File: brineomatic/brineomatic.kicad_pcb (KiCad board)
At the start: 4 copper layers, 106 x 66.5 mm, 168 parts, among them J1 Conn_01x04_MountingPin, J10 5.08MM, J12 3.5MM, J14 3.5MM, J16 3.5MM, J19 USB_TYPE_C_16PIN, J20 Conn_01x04, J22 3.5mm, J24 3.5MM, J7 3.5MM, Q1 AO3400A, Q2 AO3400A, Q3 20N06, Q4 AO3400A, Q5 AO3400A, Q6 AO3400A, Q7 AO3400A, SW1 RESET, SW2 BOOT, U1 ADS1115IDGSR, U2 LM74700, U3 XL1509-5.0, U4 ESP32-S3-WROOM-1-N16R8, U5 USBLC6-2SC6, U6 SN74LV1T34DBV, U7 XC6210B332MR, U8 TMC2209-LA, U9 MAX3485

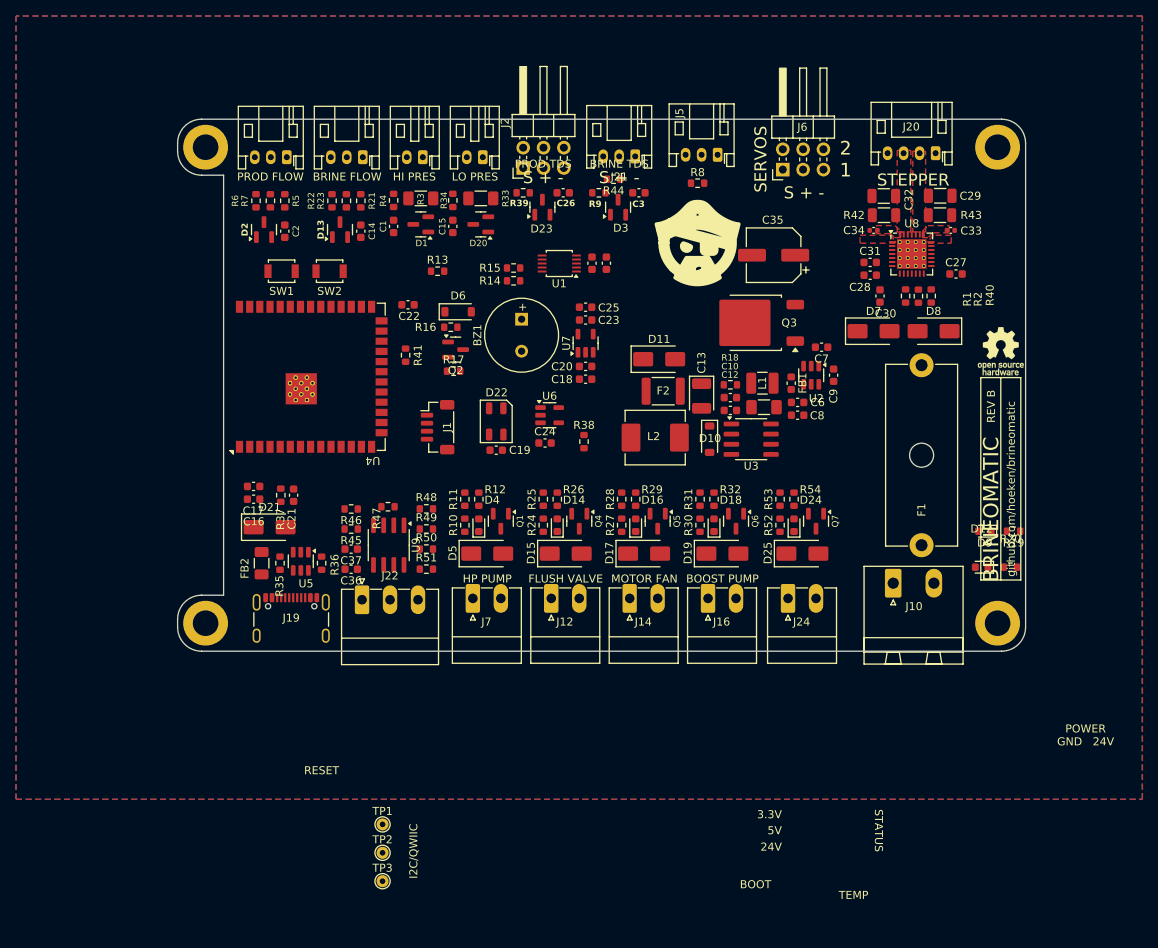
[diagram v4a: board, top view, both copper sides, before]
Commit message: all connectors are now flush withe 3mm outside edge of the case
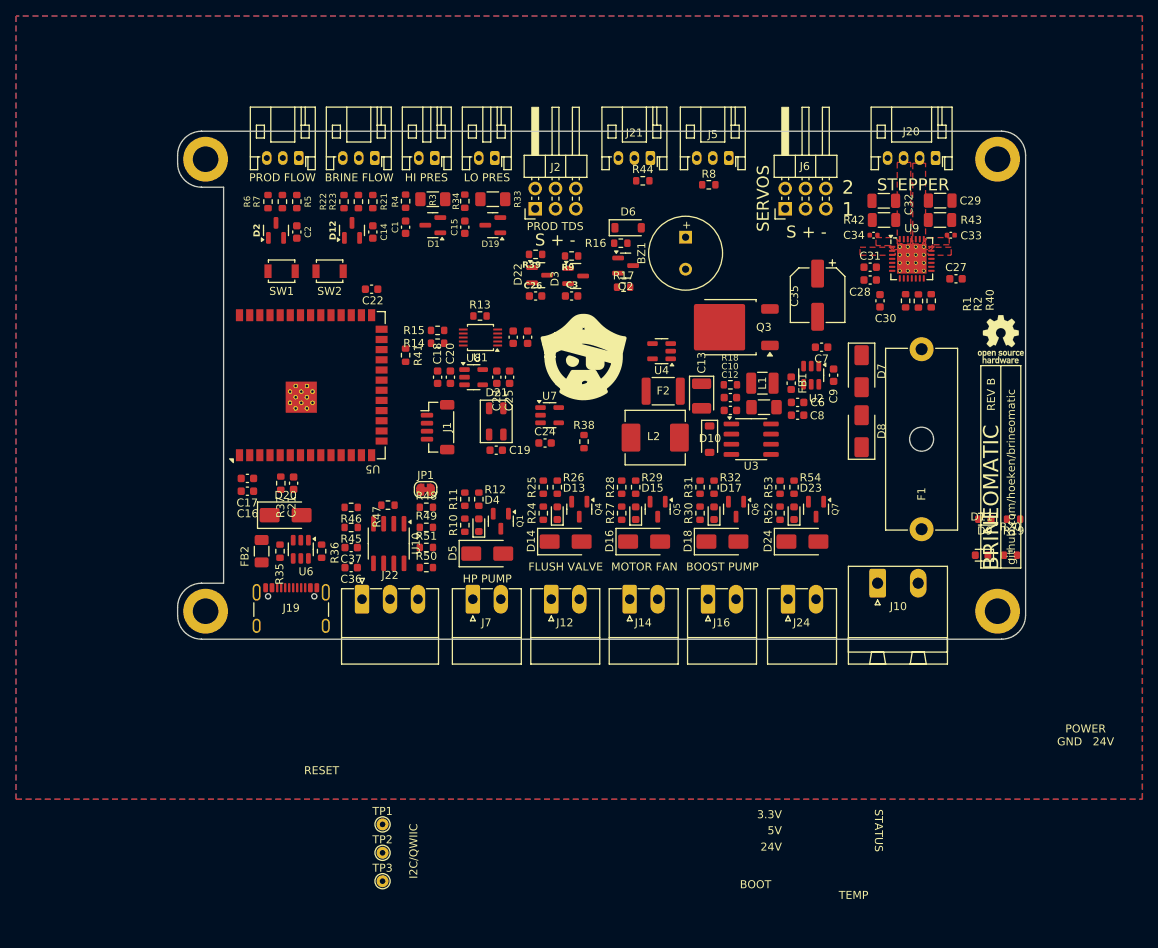
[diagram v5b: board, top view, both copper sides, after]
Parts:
- removed the D11 at (123.2, 57.5)
- added JP1: SolderJumper_2_Bridged, Jumper:SolderJumper-2_P1.3mm_Bridged_RoundedPad1.0x1.5mm, F.Cu at (94.0, 73.8)
- added U4: MAX40200AUK, Package_TO_SOT_SMD:SOT-23-5, F.Cu at (123.5, 56.5)
- moved D6 23.7 mm to (119.3, 41.1)
- moved Q2 23.7 mm to (119.0, 45.8)
- moved R16 23.7 mm to (118.4, 43.0)
- moved R17 23.7 mm to (118.8, 48.5)
- moved BZ1 22.9 mm to (126.5, 44.2)
- moved SYM2 20.2 mm to (113.8, 57.2)
- moved C18 18.5 mm to (95.5, 59.8), turned to -90 degrees
- moved C20 17.0 mm to (97.1, 59.8), turned to -90 degrees
- moved D8 15.4 mm to (148.5, 66.5), turned to 90 degrees
- moved C3 15.4 mm to (112.2, 49.6), turned to 180 degrees
- moved U8 14.6 mm to (100.0, 59.8), turned to 0 degrees
- moved C4 13.5 mm to (105.0, 54.8)
- moved C5 13.5 mm to (106.8, 54.8)
- moved U1 13.5 mm to (100.9, 54.8)
- moved C26 13.4 mm to (107.8, 49.6), turned to 180 degrees
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- renumbered D12 to D11, D13 to D12, D14 to D13, D15 to D14, D16 to D15, D17 to D16, D18 to D17, D19 to D18, D20 to D19, D21 to D20, D22 to D21, D23 to D22, D24 to D23, D25 to D24, R51 to R50, R50 to R51, U9 to U10, U4 to U5, U5 to U6, U6 to U7, U7 to U8, U8 to U9
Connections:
- C13 pad 1: 5V_TRUE -> 5V_HIGH_POWER
- F2 pad 1: 5V_TRUE -> 5V_HIGH_POWER
- J11 pad 1: 5V_TRUE -> +5V
- J2 pad 3: 5V_TRUE -> +5V
- J2 pad 4: 5V_TRUE -> +5V
- J4 pad 1: 5V_TRUE -> +5V
- J6 pad 3: 5V_TRUE -> 5V_HIGH_POWER
- J6 pad 4: 5V_TRUE -> 5V_HIGH_POWER
- R21 pad 2: 5V_TRUE -> +5V
- R5 pad 2: 5V_TRUE -> +5V
- R51 pad 2: Net-(J22-Pin_1) -> Net-(JP1-A)
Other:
- board size 106 x 66.5 mm -> 106 x 63.5 mm
- board text removed: "BRINE TDS"

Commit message: connector placement done
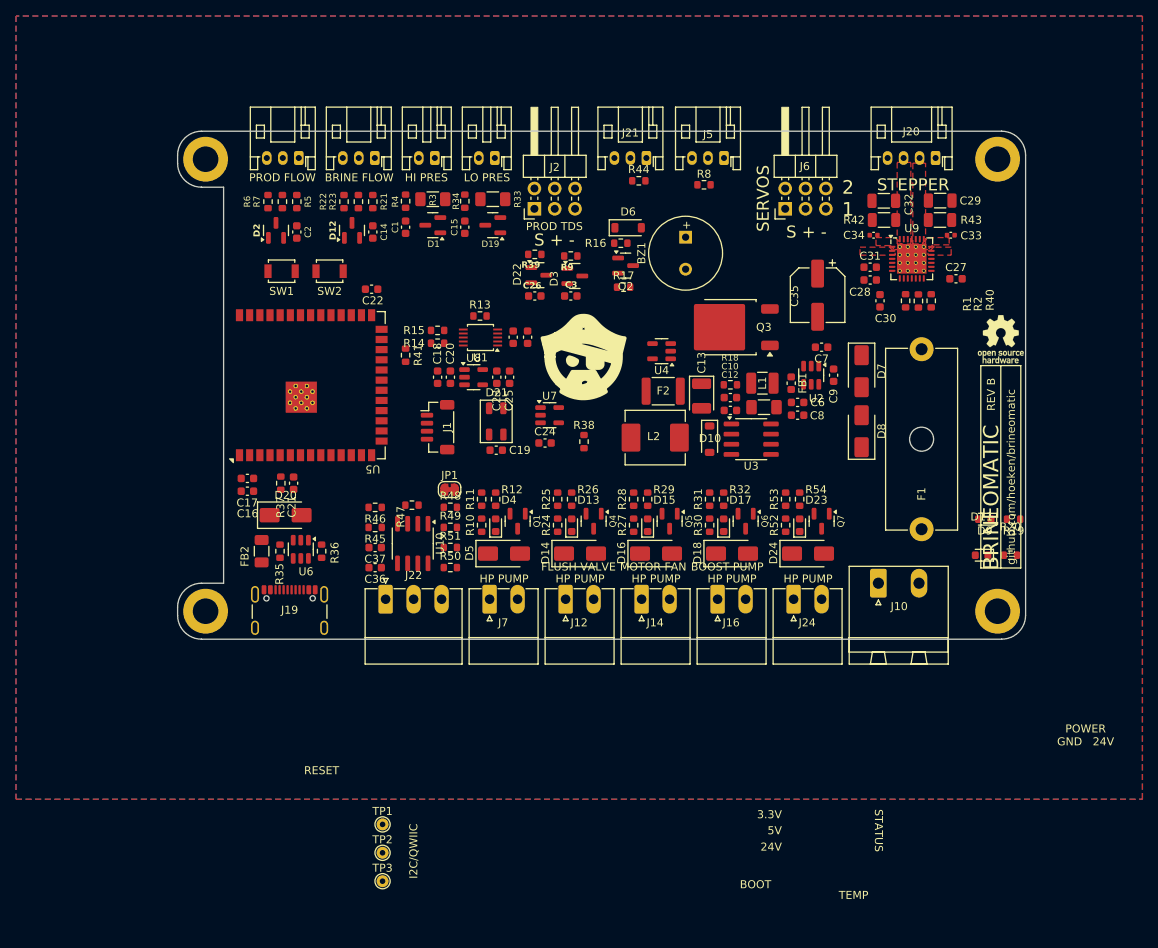
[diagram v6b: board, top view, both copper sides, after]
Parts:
- moved C36 3.00 mm to (87.7, 83.6)
- moved C37 3.00 mm to (87.7, 81.0)
- moved JP1 3.00 mm to (97.0, 73.8)
- moved R45 3.00 mm to (87.7, 78.5)
- moved R46 3.00 mm to (87.7, 76.0)
- moved R47 3.00 mm to (92.3, 75.7)
- moved R48 3.00 mm to (97.1, 76.0)
- moved R49 3.00 mm to (97.1, 78.5)
- moved R50 3.00 mm to (97.1, 83.5)
- moved R51 3.00 mm to (97.1, 81.0)
- moved U10 3.00 mm to (92.4, 80.5)
- moved J22 2.94 mm to (89.0, 87.5)
- moved D13 2.34 mm to (112.3, 78.2)
- moved D14 2.34 mm to (113.3, 81.8)
- moved Q4 2.34 mm to (115.0, 77.8)
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
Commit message: schematic tidy, usb c position verified, component placement work.
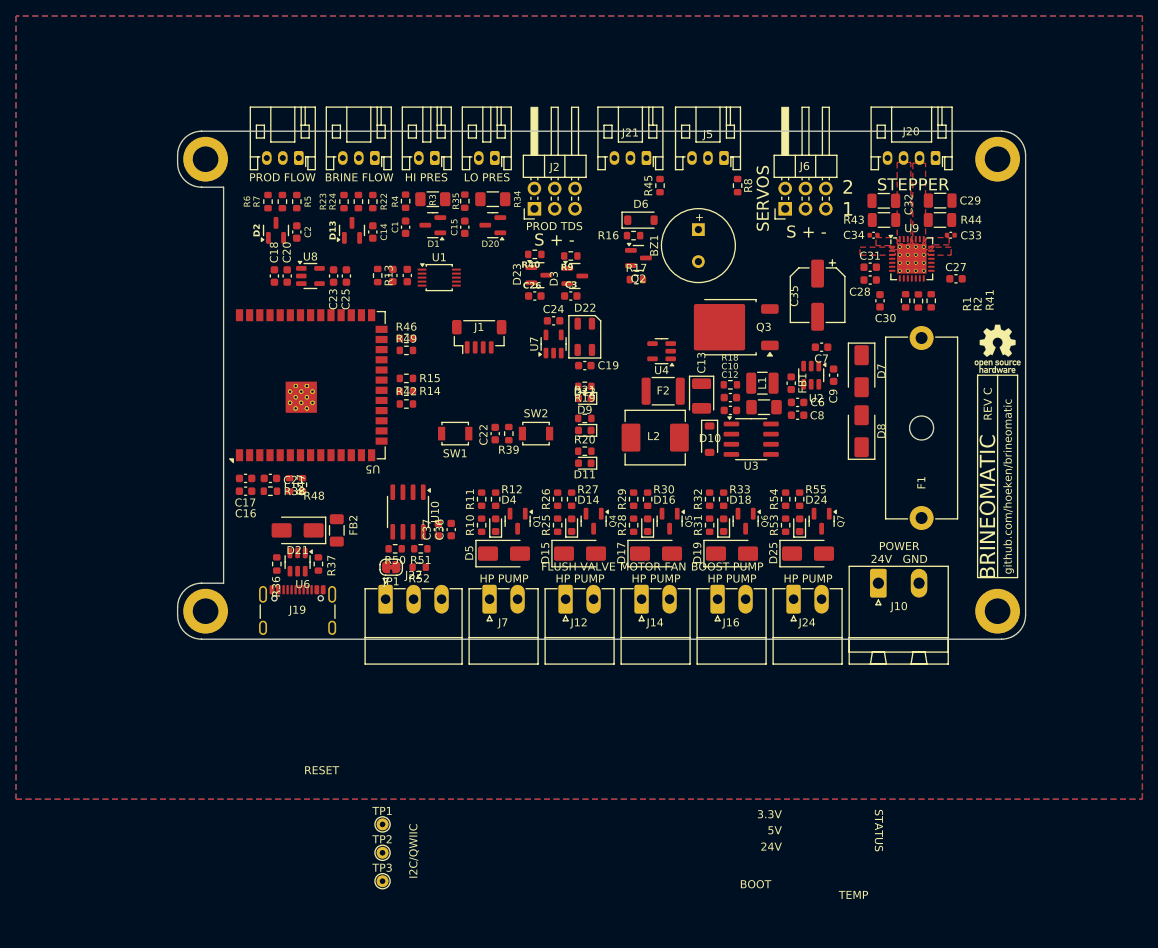
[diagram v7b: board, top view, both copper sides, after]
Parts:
- removed SYM2: Logo_Open_Hardware_Small, yarrboard:Logo Small
- added D11: GREEN, LED_SMD:LED_0603_1608Metric, F.Cu at (113.9, 70.5)
- added R20: 10k, Resistor_SMD:R_0603_1608Metric, F.Cu at (113.9, 69.0)
- R50: renamed from R49; value 10k -> 20k
- R51: renamed from R50; value 10k -> 20k
- moved R19 56.1 mm to (113.9, 60.9)
- moved R21 55.9 mm to (113.9, 64.9)
- moved D9 52.2 mm to (113.9, 62.4)
- moved D12 52.0 mm to (113.9, 66.4)
- moved SW2 32.8 mm to (107.8, 66.8), turned to 0 degrees
- moved SW1 29.7 mm to (97.7, 66.8)
- moved C18 24.0 mm to (75.1, 47.1)
- moved C23 24.0 mm to (82.5, 47.1)
- moved C25 24.0 mm to (84.1, 47.1)
- moved U8 24.0 mm to (79.6, 47.1)
- moved C20 24.0 mm to (76.7, 47.1)
- moved R46 24.0 mm to (91.6, 54.9), turned to 0 degrees
- moved C22 23.8 mm to (102.7, 66.8), turned to 90 degrees
- moved R49 20.4 mm to (91.6, 56.4)
- moved C5 18.5 mm to (89.9, 47.0), turned to -90 degrees
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- renumbered D11 to D12, D12 to D13, D13 to D14, D14 to D15, D15 to D16, D16 to D17, D17 to D18, D18 to D19, D19 to D20, D20 to D21, D21 to D22, D22 to D23, D23 to D24, D24 to D25, R20 to R21, R21 to R22, R22 to R23, R23 to R24, R24 to R25, R25 to R26, R26 to R27, R27 to R28, R28 to R29, R29 to R30, R30 to R31, R31 to R32, R32 to R33, R33 to R34, R34 to R35, R35 to R36, R36 to R37, R37 to R38, R38 to R39, R39 to R40, R40 to R41, R41 to R42, R42 to R43, R43 to R44, R44 to R45, R45 to R46, R46 to R47, R47 to R48, R48 to R49, R51 to R52, R52 to R53, R53 to R54, R54 to R55
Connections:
- net /ESP32-S3/GPIO16 renamed SOLENOID5
- net GPIO5 renamed RS485_DERE
- R16 pad 2: /Piezo/PIEZO -> /ESP32-S3/GPIO15
- R46 pad 1: GPIO47 -> RS485_DI
- R49 pad 1: GPIO48 -> RS485_RO
- U10 pad 1: GPIO48 -> RS485_RO
- U10 pad 4: GPIO47 -> RS485_DI
- U5 pad 24: GPIO47 -> RS485_RO
- U5 pad 25: GPIO48 -> RS485_DI
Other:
- board text added: "POWER 24V GND"
- board text added: "REV C"
- board text removed: "POWER GND 24V"
- board text removed: "REV B"

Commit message: added voltage divider to vref.  more component shuffling.
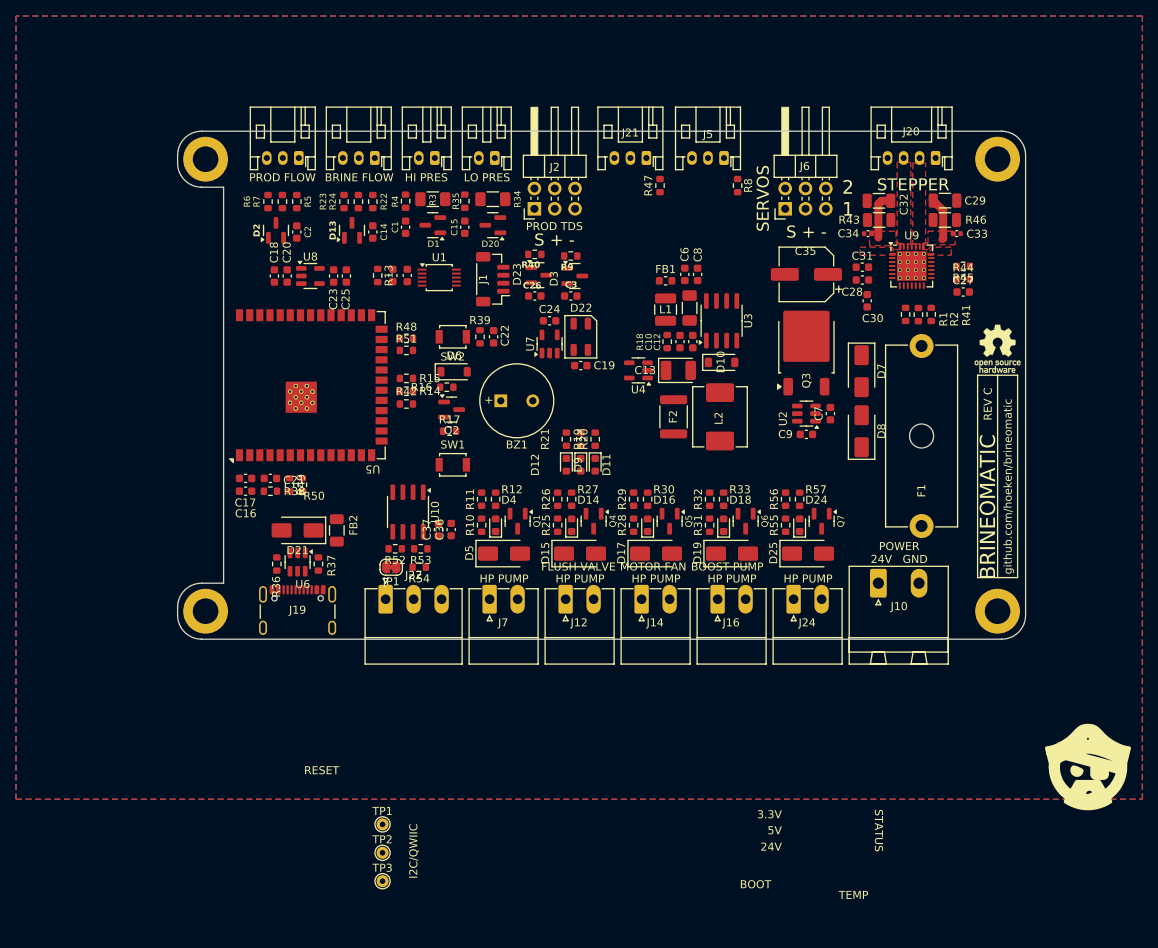
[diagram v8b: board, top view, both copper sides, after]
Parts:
- added R44: 20k, Resistor_SMD:R_0603_1608Metric, F.Cu at (161.2, 47.5)
- added R45: 10k, Resistor_SMD:R_0603_1608Metric, F.Cu at (161.2, 45.9)
- added SYM2: Logo_Open_Hardware_Small, yarrboard:Logo Small, F.Cu at (176.8, 108.5)
- moved D6 30.1 mm to (97.6, 59.1)
- moved R16 30.1 mm to (96.7, 61.0)
- moved R17 30.1 mm to (97.0, 66.5)
- moved Q2 30.1 mm to (97.2, 63.8)
- moved BZ1 29.9 mm to (105.4, 62.7), turned to 0 degrees
- moved C8 21.6 mm to (128.0, 46.9), turned to 90 degrees
- moved C6 21.3 mm to (126.4, 46.9), turned to 90 degrees
- moved FB1 20.3 mm to (124.0, 47.7), turned to 0 degrees
- moved SW2 16.0 mm to (97.4, 54.7), turned to 180 degrees
- moved C11 15.5 mm to (127.0, 51.1), turned to 90 degrees
- moved U3 15.3 mm to (131.0, 52.7), turned to 90 degrees
- moved L1 15.2 mm to (124.0, 51.3), turned to -90 degrees
- moved R39 12.6 mm to (100.8, 54.7), turned to 90 degrees
- moved C22 12.1 mm to (102.5, 54.7), turned to -90 degrees
- moved Q3 9.90 mm to (141.6, 55.9), turned to 90 degrees
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- renumbered R44 to R46, R45 to R47, R46 to R48, R47 to R49, R48 to R50, R49 to R51, R50 to R52, R51 to R53, R52 to R54, R53 to R55, R54 to R56, R55 to R57
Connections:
- U9 pad 17: unconnected-(U9-VREF-Pad17) -> Net-(U9-VREF)
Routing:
- net +24V: track 0.00 -> 11.3 mm
